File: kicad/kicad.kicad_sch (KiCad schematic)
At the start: 10 parts, among them U1 LM317_TO-220, U2 LM317_TO-220, U3 LM317_TO-220

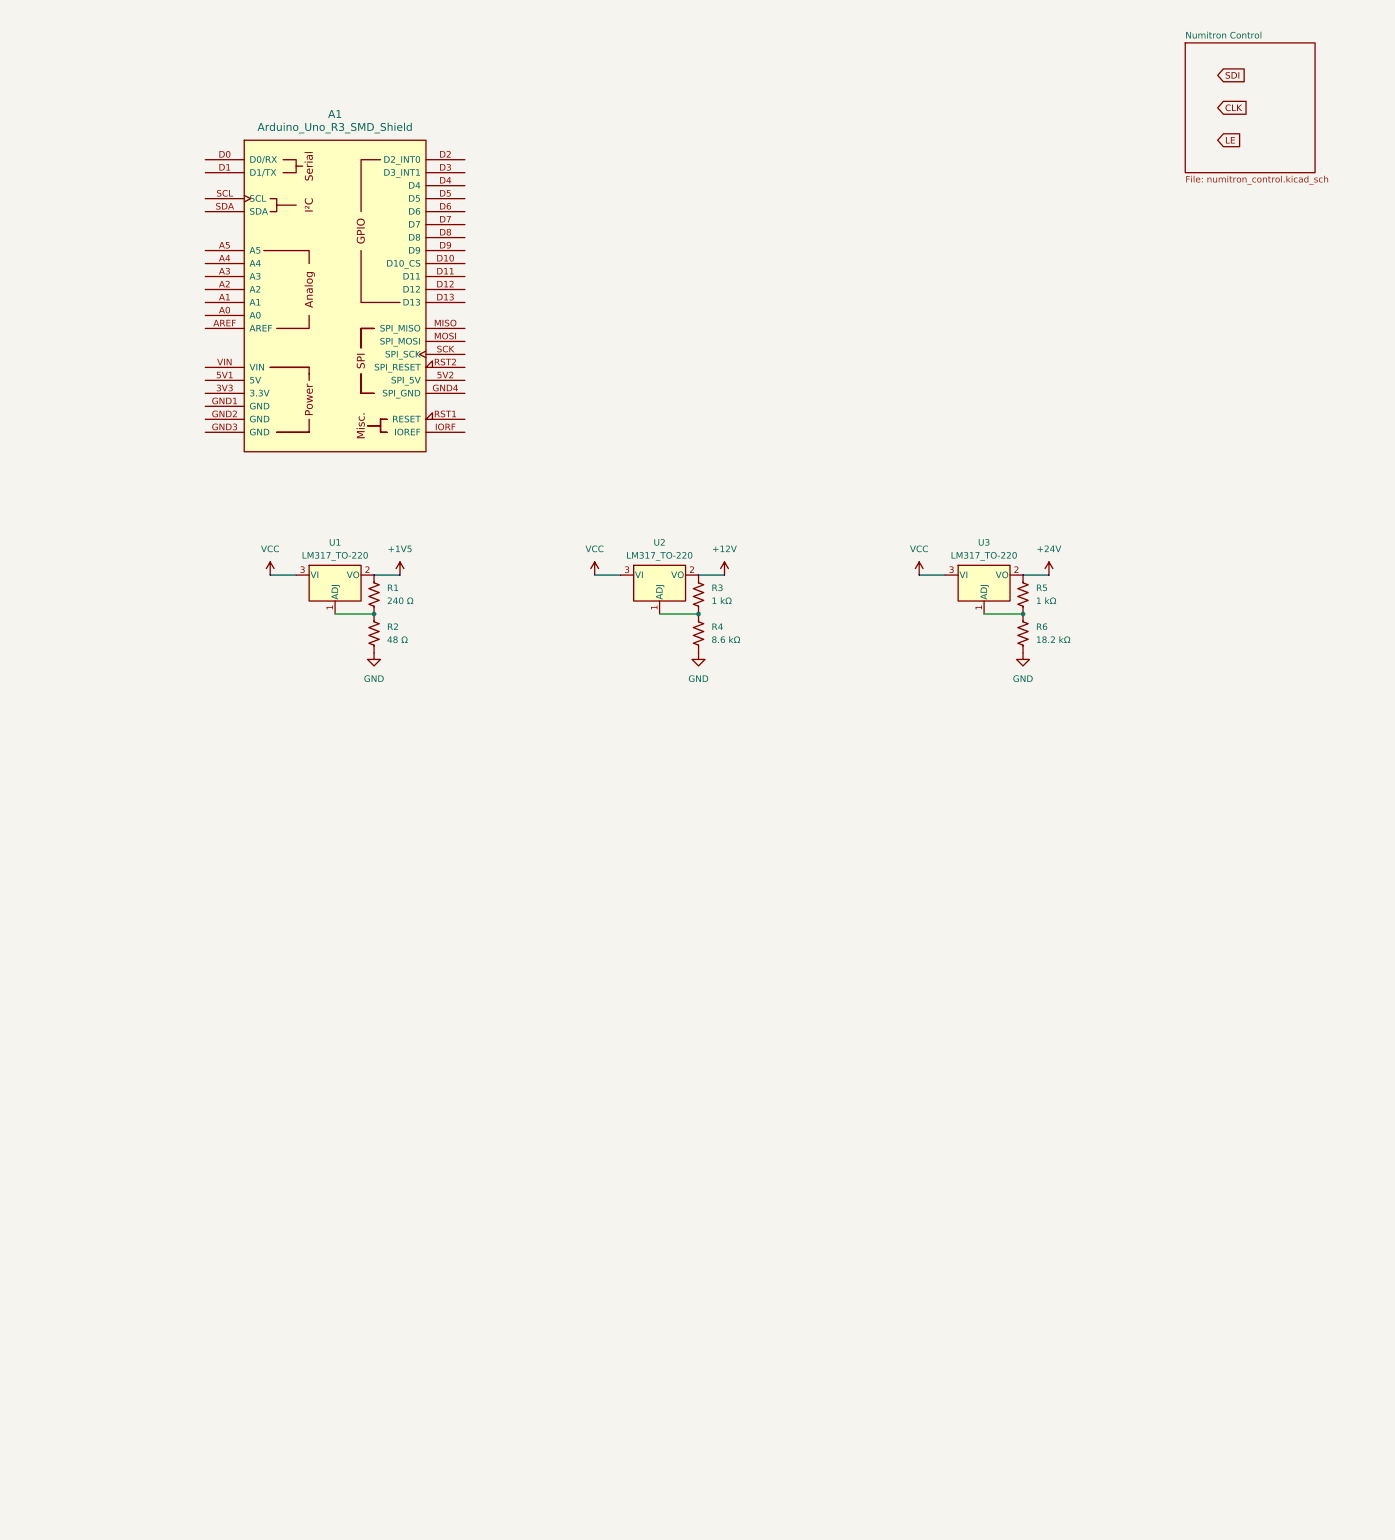
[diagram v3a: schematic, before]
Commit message: Updated driver breakout and selected boost IC
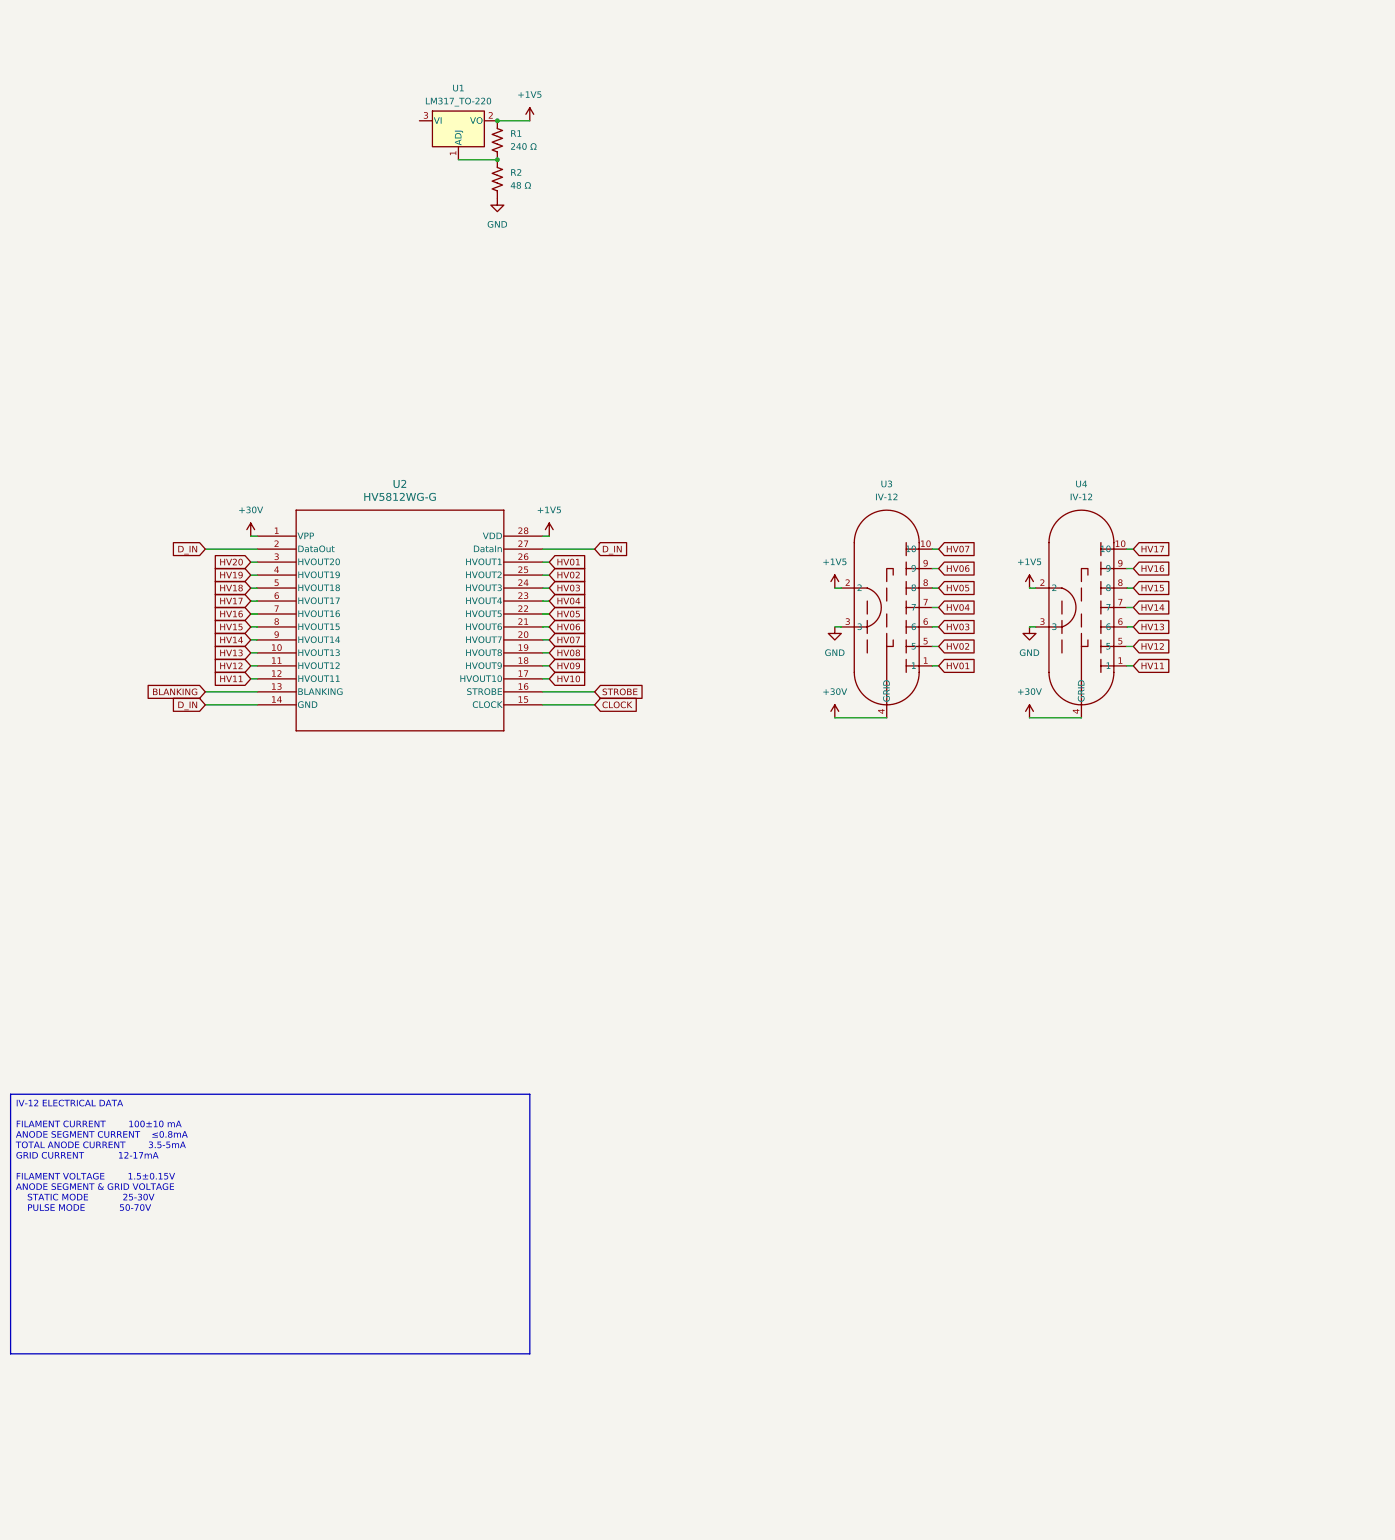
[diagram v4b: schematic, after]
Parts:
- removed A1: Arduino_Uno_R3_SMD_Shield, PCM_arduino-library:Arduino_Uno_R3_Shield, symbol PCM_arduino-library:Arduino_Uno_R3_SMD_Shield
- removed R3, R5: 1 kΩ, symbol Device:R_US
- removed R4: 8.6 kΩ, symbol Device:R_US
- removed R6: 18.2 kΩ, symbol Device:R_US
- removed U2, U3: LM317_TO-220, Package_TO_SOT_THT:TO-220-3_Vertical, symbol Regulator_Linear:LM317_TO-220
- added U2: HV5812WG-G, SOW28_17P90X7P50_MCH, symbol New_Library:HV5812WG-G
- added U3, U4: IV-12, symbol New_Library:IV-12
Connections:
- net +1V5: now also R1.1, U1.2 (VO), U2.28 (VDD), U3.2, U4.2
- net GND: now also U3.3, U4.3
- new net +30V: U2.1 (VPP), U3.4 (GRID), U4.4 (GRID)
- new net BLANKING: U2.13 (BLANKING)
- new net CLOCK: U2.15 (CLOCK)
- new net D_IN: U2.14 (GND), U2.2 (DataOut), U2.27 (DataIn)
- new net HV01: U2.26 (HVOUT1), U3.1
- new net HV02: U2.25 (HVOUT2), U3.5
- new net HV03: U2.24 (HVOUT3), U3.6
- new net HV04: U2.23 (HVOUT4), U3.7
- new net HV05: U2.22 (HVOUT5), U3.8
- new net HV06: U2.21 (HVOUT6), U3.9
- new net HV07: U2.20 (HVOUT7), U3.10
- new net HV08: U2.19 (HVOUT8)
- new net HV09: U2.18 (HVOUT9)
- new net HV10: U2.17 (HVOUT10)
- new net HV11: U2.12 (HVOUT11), U4.1
- new net HV12: U2.11 (HVOUT12), U4.5
- new net HV13: U2.10 (HVOUT13), U4.6
- new net HV14: U2.9 (HVOUT14), U4.7
- new net HV15: U2.8 (HVOUT15), U4.8
- new net HV16: U2.7 (HVOUT16), U4.9
- new net HV17: U2.6 (HVOUT17), U4.10
- new net HV18: U2.5 (HVOUT18)
- new net HV19: U2.4 (HVOUT19)
- new net HV20: U2.3 (HVOUT20)
- new net STROBE: U2.16 (STROBE)
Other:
- removed sheet Numitron Control
- title: NUMITRON CLOCK -> IV-12 NUMITRON DRIVER
